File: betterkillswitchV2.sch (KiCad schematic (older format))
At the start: 13 parts, among them J1 Conn_01x04, K1 MainRelay, Q1 IRL540, SW2 Bussmann CB285-80, U2 LM2596Module, U3 74LS32

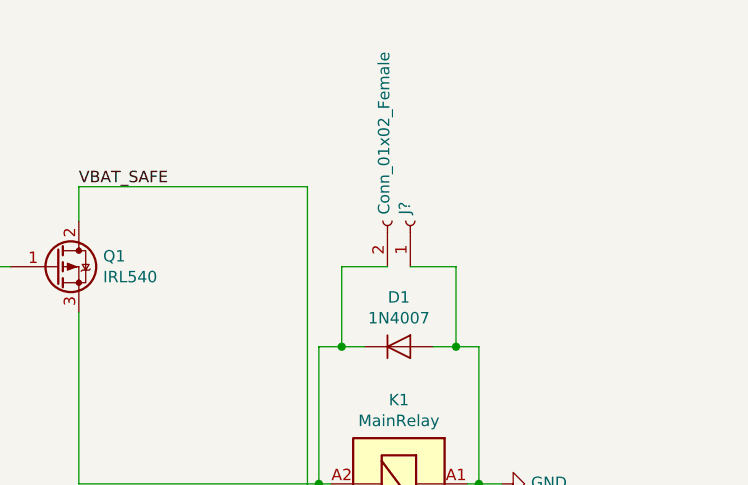
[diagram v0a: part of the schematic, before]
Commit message: added package for relay
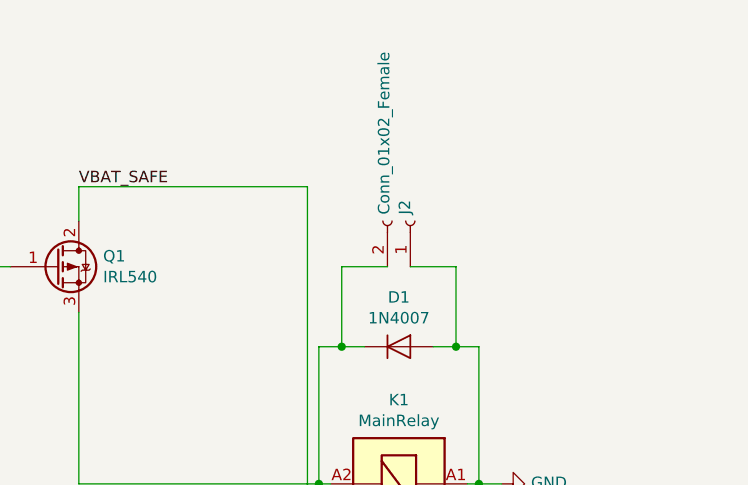
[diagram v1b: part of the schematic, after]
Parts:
- J2: renamed from J?; footprint (none) -> Connector_PinHeader_2.54mm:PinHeader_1x02_P2.54mm_Vertical
- K1: footprint Relay_THT:Relay_SPST_Finder_32.21-x300 -> (none)
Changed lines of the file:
@@
 F 0 "K1" V 6883 3250 50  0000 C CNN
 F 1 "MainRelay" V 6974 3250 50  0000 C CNN
-F 2 "Relay_THT:Relay_SPST_Finder_32.21-x300" H 8720 3220 50  0001 C CNN
+F 2 "" H 8720 3220 50  0001 C CNN
 F 3 "http://gfinder.findernet.com/assets/Series/355/S32EN.pdf" H 7450 3250 50  0001 C CNN
 	1    7450 3250
@@
 	7800 3050 7900 3050
 $Comp
-L Connector:Conn_01x02_Female J?
+L Connector:Conn_01x02_Female J2
 U 1 1 604C06B3
 P 7500 1900
-F 0 "J?" H 7528 1876 50  0000 L CNN
+F 0 "J2" H 7528 1876 50  0000 L CNN
 F 1 "Conn_01x02_Female" H 7528 1785 50  0000 L CNN
-F 2 "" H 7500 1900 50  0001 C CNN
+F 2 "Connector_PinHeader_2.54mm:PinHeader_1x02_P2.54mm_Vertical" H 7500 1900 50  0001 C CNN
 F 3 "~" H 7500 1900 50  0001 C CNN
 	1    7500 1900
